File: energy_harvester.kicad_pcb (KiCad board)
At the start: 2 copper layers, 13 parts, among them IC1 LTC3108EGN-1-PBF, J1 Conn_01x02_Female, J2 Conn_01x02_Female, Q1 RUM002N02T2L

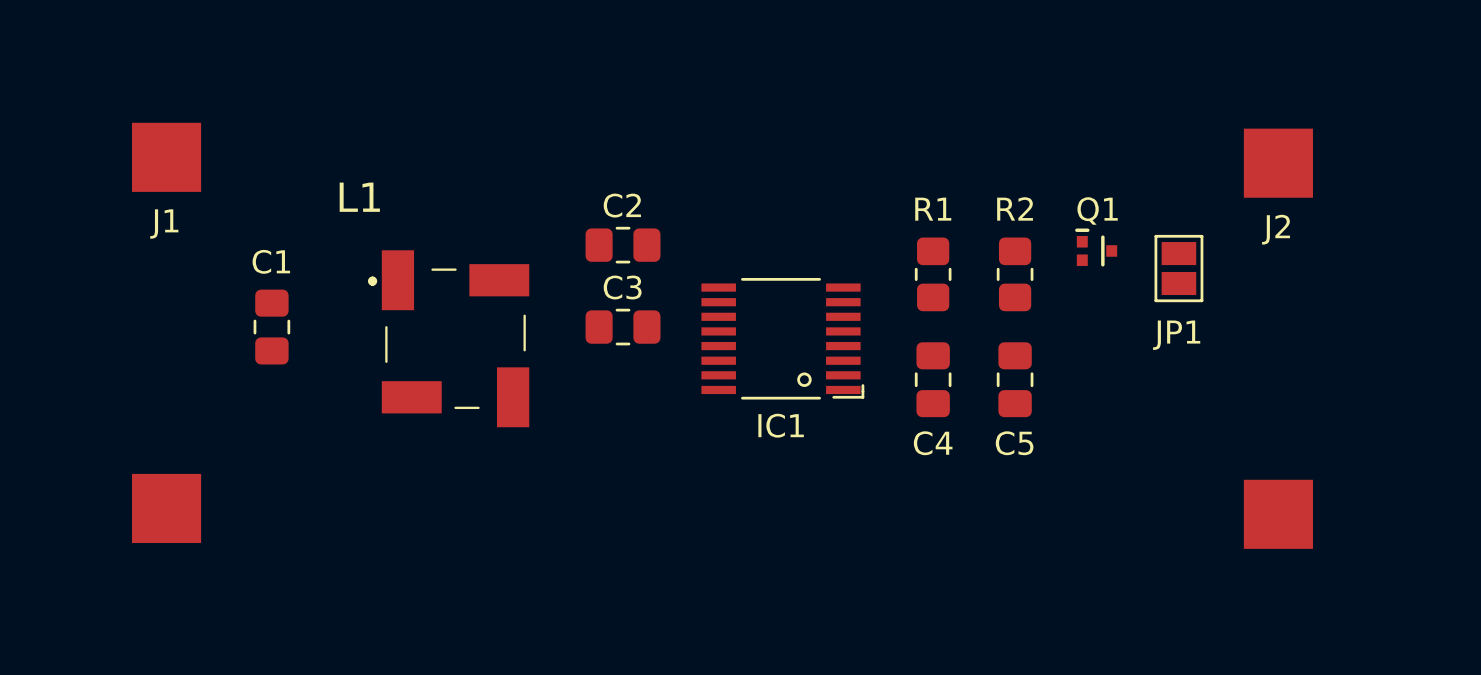
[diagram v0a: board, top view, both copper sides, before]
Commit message: Add traces, step files, corr in schematic
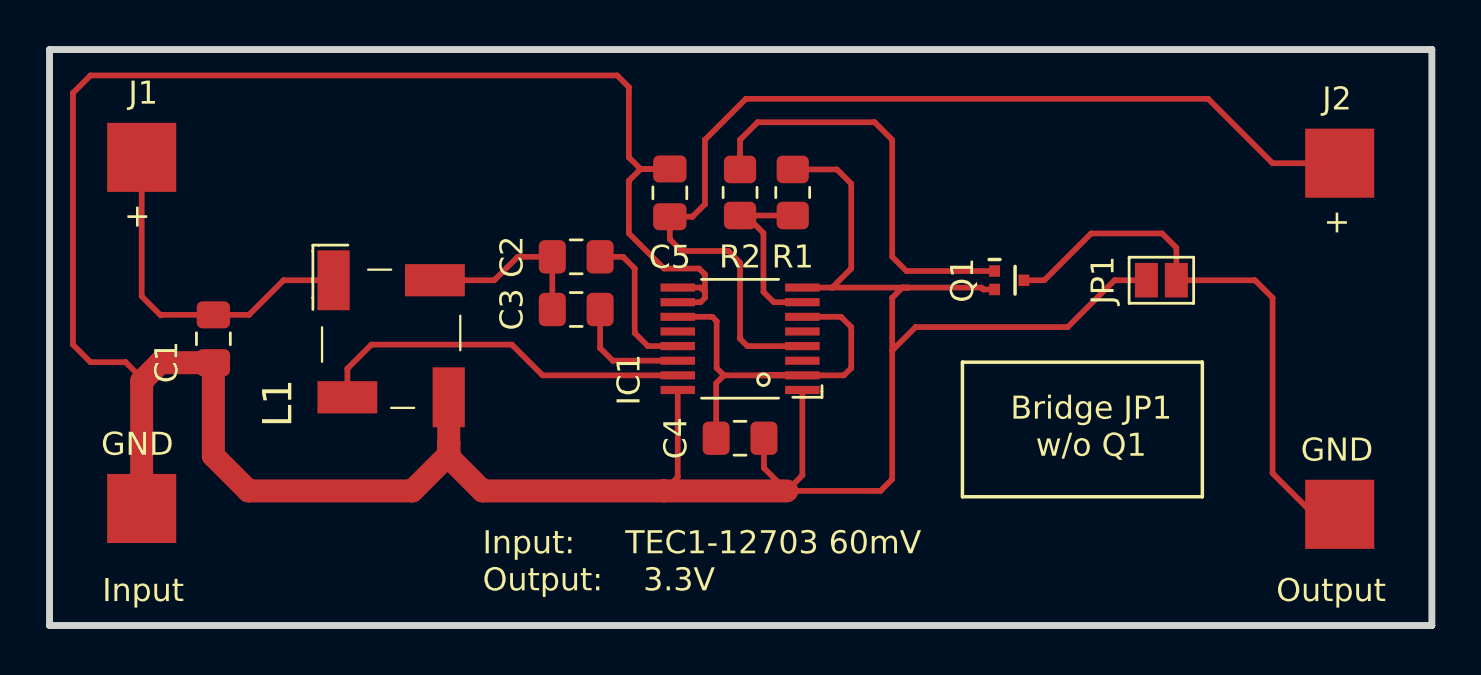
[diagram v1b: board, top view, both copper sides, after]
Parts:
- moved C5 17.0 mm to (120.9, 82.8), turned to 90 degrees
- moved R2 12.5 mm to (124.0, 82.8)
- moved C4 8.76 mm to (124.0, 93.5), turned to 0 degrees
- moved R1 7.06 mm to (126.2, 82.8)
- moved Q1 4.02 mm to (135.6, 86.6)
- moved L1 2.79 mm to (108.5, 89.2)
- moved J2 2.66 mm to (150.0, 89.2), turned to -90 degrees
- moved C1 2.59 mm to (101.1, 89.2)
- moved C3 2.17 mm to (116.8, 87.9)
- moved C2 2.09 mm to (116.8, 85.6)
- moved IC1 1.78 mm to (124.0, 89.2)
- moved J1 1.08 mm to (98.0, 88.9)
- moved JP1 0.92 mm to (142.2, 86.6), turned to 180 degrees
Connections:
- C2 pad 1: Net-(C1-Pad1) -> Net-(C2-Pad1)
- C3 pad 1: Net-(C1-Pad1) -> Net-(C2-Pad1)
- L1 pad 4: Net-(C1-Pad1) -> Net-(C2-Pad1)
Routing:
- net GND: track 0.00 -> 153.2 mm
- net /VOUT: track 0.00 -> 44.6 mm
- net Net-(J2-Pad2): track 0.00 -> 24.9 mm
- net /VAUX: track 0.00 -> 18.7 mm
- net Net-(Q1-Pad1): track 0.00 -> 18.3 mm
- net /SW: track 0.00 -> 16.6 mm
- net Net-(C1-Pad1): track 0.00 -> 15.3 mm
- net Net-(C2-Pad1): track 0.00 -> 7.80 mm
- net /PGD: track 0.00 -> 7.79 mm
- net /C1: track 0.00 -> 6.61 mm
- net /C2: track 0.00 -> 5.27 mm
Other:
- board outline added: 60 x 25 mm
- board text added: "+"
- board text added: "Bridge JP1 w/o Q1"
- board text added: "GND"
- board text added: "Input"
- board text added: "Input: TEC1-12703 60mV Output: 3.3V"
- board text added: "Output"

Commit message: Add silkscreen desc
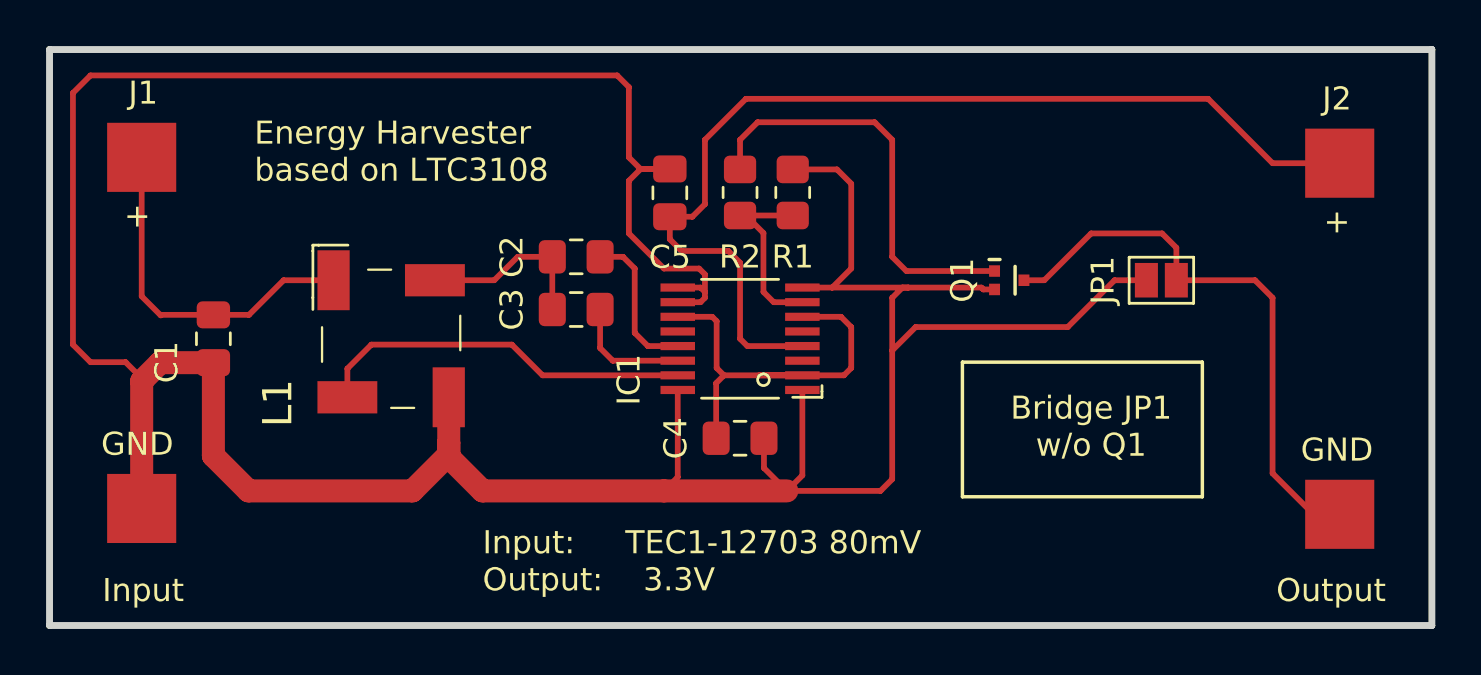
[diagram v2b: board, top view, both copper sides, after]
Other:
- board text added: "Energy Harvester based on LTC3108"
- board text added: "Input: TEC1-12703 80mV Output: 3.3V"
- board text removed: "Input: TEC1-12703 60mV Output: 3.3V"
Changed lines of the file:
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@@
   (gr_line locked (start 153.98 76.6) (end 153.98 101.6) (layer "Edge.Cuts") (width 0.3))
   (gr_line locked (start 93.98 101.6) (end 93.98 76.6) (layer "Edge.Cuts") (width 0.3))
-  (gr_text "Input: 	TEC1-12703 60mV\nOutput:	3.3V" (at 112.776 98.806) (layer "F.SilkS")
+  (gr_text "Input: 	TEC1-12703 80mV\nOutput:	3.3V" (at 112.776 98.806) (layer "F.SilkS")
     (effects (font (size 1 1) (thickness 0.15)) (justify left))
   )
@@
     (effects (font (size 1 1) (thickness 0.15)))
   )
+  (gr_text "Energy Harvester \nbased on LTC3108" (at 102.87 81.026) (layer "F.SilkS")
+    (effects (font (size 1 1) (thickness 0.15)) (justify left))
+  )
   (gr_text "GND" (at 149.86 93.98) (layer "F.SilkS")
